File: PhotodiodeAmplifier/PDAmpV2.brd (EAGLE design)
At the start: 50.8 x 30.1 mm, 21 parts, among them IC1 CA3140N, IC2 7812L

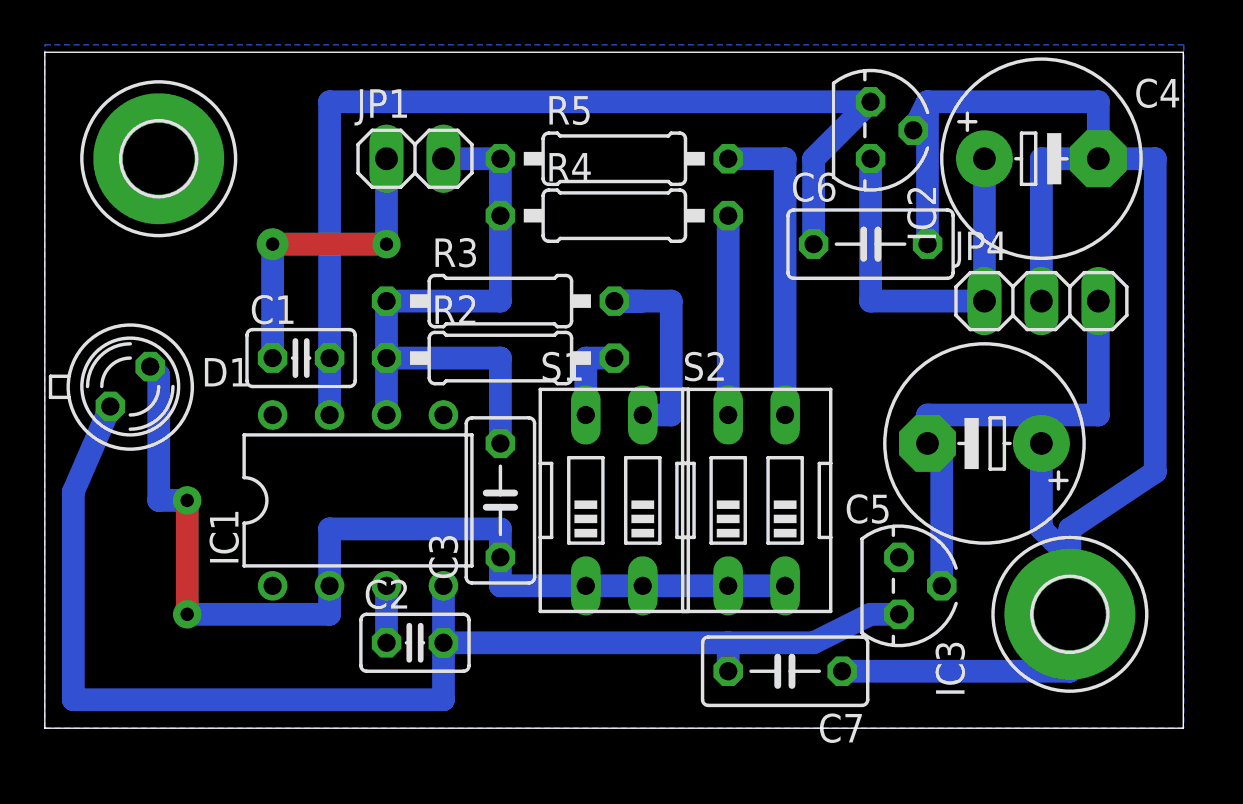
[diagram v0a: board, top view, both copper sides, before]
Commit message: Insert 50 ohm resistor into output
This actually makes the circuit work properly, previously I was doing this
with a terminator, but that's a bit dangerous for your ICS
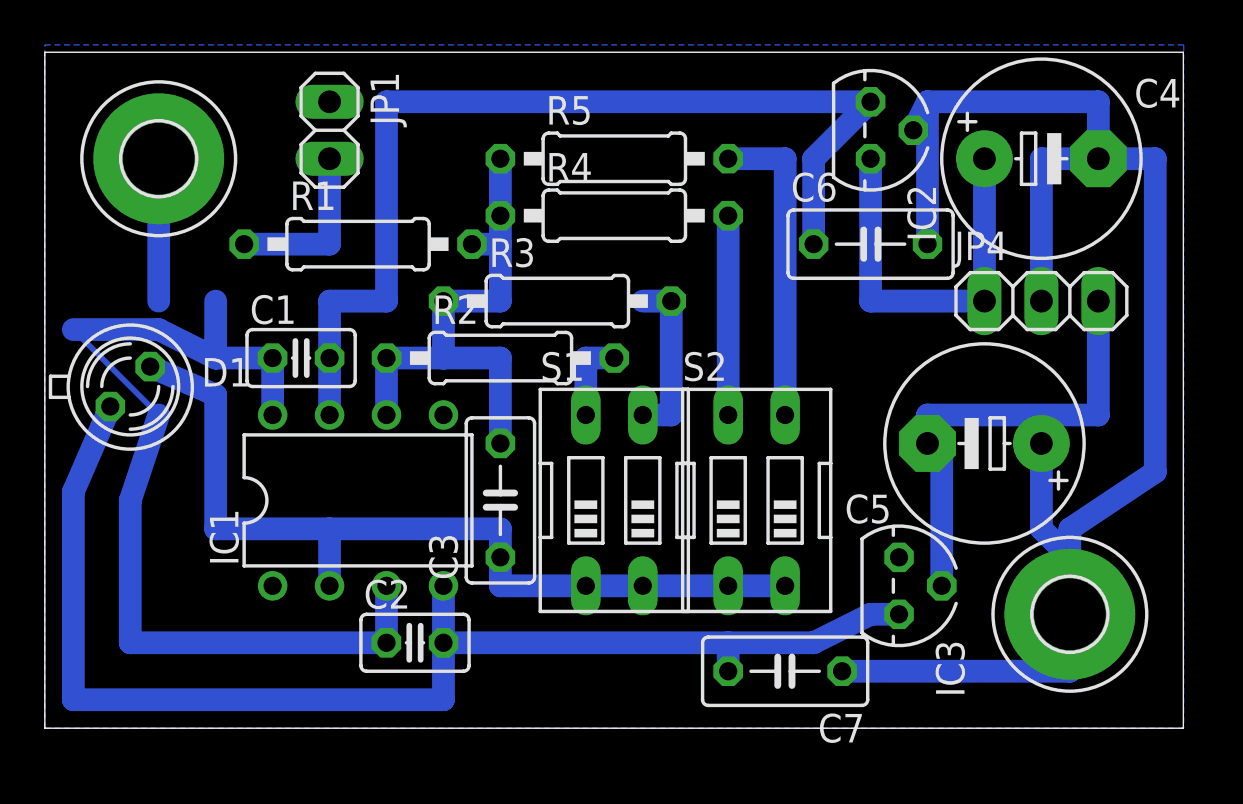
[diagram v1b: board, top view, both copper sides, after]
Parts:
- added R1: (no value), resistor:0207/10
- moved JP1 4.02 mm to (12.7, 26.7), turned to 270 degrees
- moved R3 2.54 mm to (22.9, 19.1)
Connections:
- new net N$10: JP1.2, R1.1
- net N$16: now also R1.2; no longer JP1.2
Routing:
- net GND: track 89.1 -> 122.9 mm
- net N$10: track 0.00 -> 7.62 mm
- net N$4: track 45.5 -> 39.6 mm
- net N$16: track 27.9 -> 24.1 mm
- net N$13: track 10.2 -> 7.62 mm
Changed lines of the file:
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@@
 </autorouter>
 <elements>
-<element name="JP1" library="pinhead" package="1X02" value="" x="16.51" y="25.4"/>
+<element name="JP1" library="pinhead" package="1X02" value="" x="12.7" y="26.67" rot="R270"/>
 <element name="GND" library="holes" package="3,2-PAD" value="MOUNT-PAD-ROUND3.2" x="5.08" y="25.4"/>
 <element name="H2" library="holes" package="3,2-PAD" value="MOUNT-PAD-ROUND3.2" x="45.72" y="5.08"/>
@@
 <element name="C3" library="rcl" package="C050-030X075" value="" x="20.32" y="10.16" rot="R90"/>
 <element name="R2" library="resistor" package="0207/10" value="" x="20.32" y="16.51"/>
-<element name="R3" library="resistor" package="0207/10" value="" x="20.32" y="19.05"/>
+<element name="R3" library="resistor" package="0207/10" value="" x="22.86" y="19.05"/>
 <element name="R4" library="resistor" package="0207/10" value="" x="25.4" y="22.86"/>
 <element name="R5" library="resistor" package="0207/10" value="" x="25.4" y="25.4"/>
+<element name="R1" library="resistor" package="0207/10" value="" x="13.97" y="21.59"/>
 </elements>
 <signals>
@@
 <contactref element="H2" pad="B3,2"/>
 <contactref element="JP1" pad="1"/>
-<wire x1="15.24" y1="6.35" x2="15.24" y2="3.81" width="1.016" layer="16"/>
 <wire x1="38.735" y1="26.67" x2="39.37" y2="27.94" width="1.016" layer="16"/>
 <polygon width="0.8128" layer="16">
@@
 <wire x1="49.53" y1="11.43" x2="49.53" y2="25.4" width="1.016" layer="16"/>
 <wire x1="49.53" y1="25.4" x2="46.99" y2="25.4" width="1.016" layer="16"/>
-<wire x1="15.24" y1="21.59" x2="10.16" y2="21.59" width="1.016" layer="1"/>
-<wire x1="10.16" y1="16.51" x2="10.16" y2="21.59" width="1.016" layer="16"/>
-<wire x1="15.24" y1="25.4" x2="15.24" y2="21.59" width="1.016" layer="16"/>
 <wire x1="44.45" y1="12.7" x2="44.45" y2="8.89" width="1.016" layer="16"/>
 <wire x1="44.45" y1="8.89" x2="45.72" y2="7.62" width="1.016" layer="16"/>
 <wire x1="45.72" y1="7.62" x2="45.72" y2="5.08" width="1.016" layer="16"/>
-<wire x1="10.16" y1="21.59" x2="10.16" y2="21.59" width="0" layer="19" extent="1-16"/>
-<wire x1="15.24" y1="21.59" x2="15.24" y2="21.59" width="0" layer="19" extent="1-16"/>
+<wire x1="10.16" y1="13.97" x2="10.16" y2="16.51" width="1.016" layer="16"/>
+<wire x1="10.16" y1="16.51" x2="7.62" y2="16.51" width="1.016" layer="16"/>
+<wire x1="7.62" y1="16.51" x2="7.62" y2="19.05" width="1.016" layer="16"/>
+<wire x1="5.08" y1="19.05" x2="5.08" y2="25.4" width="1.016" layer="16"/>
+<wire x1="15.24" y1="6.35" x2="15.24" y2="3.81" width="1.016" layer="16"/>
+<wire x1="15.24" y1="3.81" x2="3.81" y2="3.81" width="1.016" layer="16"/>
+<wire x1="3.81" y1="3.81" x2="3.81" y2="10.16" width="1.016" layer="16"/>
+<wire x1="7.62" y1="16.51" x2="5.08" y2="17.78" width="1.016" layer="16"/>
+<wire x1="5.08" y1="17.78" x2="1.27" y2="17.78" width="1.016" layer="16"/>
+<wire x1="1.27" y1="17.78" x2="5.08" y2="13.97" width="0.254" layer="16"/>
+<wire x1="5.08" y1="13.97" x2="3.81" y2="10.16" width="1.016" layer="16"/>
 </signal>
 <signal name="N$7">
@@
 <wire x1="17.78" y1="6.35" x2="17.78" y2="3.81" width="1.016" layer="16"/>
 <wire x1="17.78" y1="3.81" x2="17.78" y2="1.27" width="1.016" layer="16"/>
-<wire x1="1.27" y1="1.27" x2="17.78" y2="1.27" width="1.016" layer="16"/>
 <wire x1="2.921" y1="14.351" x2="1.27" y2="10.541" width="1.016" layer="16"/>
 <wire x1="1.27" y1="10.541" x2="1.27" y2="1.27" width="1.016" layer="16"/>
@@
 <wire x1="34.29" y1="3.81" x2="36.83" y2="5.08" width="1.016" layer="16"/>
 <wire x1="36.83" y1="5.08" x2="38.1" y2="5.08" width="1.016" layer="16"/>
+<wire x1="17.78" y1="1.27" x2="1.27" y2="1.27" width="1.016" layer="16"/>
 </signal>
 <signal name="+12V">
@@
 <contactref element="IC1" pad="7"/>
 <contactref element="C1" pad="2"/>
-<wire x1="36.83" y1="27.94" x2="12.7" y2="27.94" width="1.016" layer="16"/>
-<wire x1="12.7" y1="27.94" x2="12.7" y2="16.51" width="1.016" layer="16"/>
 <wire x1="12.7" y1="13.97" x2="12.7" y2="16.51" width="1.016" layer="16"/>
 <wire x1="36.83" y1="27.94" x2="34.29" y2="25.4" width="1.016" layer="16"/>
 <wire x1="34.29" y1="25.4" x2="34.29" y2="21.59" width="1.016" layer="16"/>
+<wire x1="36.83" y1="27.94" x2="15.24" y2="27.94" width="1.016" layer="16"/>
+<wire x1="12.7" y1="16.51" x2="12.7" y2="19.05" width="1.016" layer="16"/>
+<wire x1="12.7" y1="19.05" x2="15.24" y2="19.05" width="1.016" layer="16"/>
+<wire x1="15.24" y1="19.05" x2="15.24" y2="27.94" width="1.016" layer="16"/>
 </signal>
 <signal name="N$4">
@@
 <wire x1="26.67" y1="6.35" x2="30.48" y2="6.35" width="1.016" layer="16"/>
 <wire x1="30.48" y1="6.35" x2="33.02" y2="6.35" width="1.016" layer="16"/>
+<contactref element="D1" pad="K"/>
+<wire x1="20.32" y1="7.62" x2="20.32" y2="6.35" width="1.016" layer="16"/>
+<wire x1="20.32" y1="6.35" x2="24.13" y2="6.35" width="1.016" layer="16"/>
+<wire x1="4.699" y1="16.129" x2="7.62" y2="14.859" width="1.016" layer="16"/>
+<wire x1="7.62" y1="14.859" x2="7.62" y2="8.89" width="1.016" layer="16"/>
+<wire x1="7.62" y1="8.89" x2="12.7" y2="8.89" width="1.016" layer="16"/>
 <wire x1="12.7" y1="6.35" x2="12.7" y2="8.89" width="1.016" layer="16"/>
 <wire x1="12.7" y1="8.89" x2="20.32" y2="8.89" width="1.016" layer="16"/>
 <wire x1="20.32" y1="8.89" x2="20.32" y2="7.62" width="1.016" layer="16"/>
-<contactref element="D1" pad="K"/>
-<wire x1="20.32" y1="7.62" x2="20.32" y2="6.35" width="1.016" layer="16"/>
-<wire x1="20.32" y1="6.35" x2="24.13" y2="6.35" width="1.016" layer="16"/>
-<wire x1="4.699" y1="16.129" x2="5.08" y2="15.748" width="1.016" layer="16"/>
-<wire x1="12.7" y1="6.35" x2="12.7" y2="5.08" width="1.016" layer="16"/>
-<wire x1="5.08" y1="15.748" x2="5.08" y2="10.16" width="1.016" layer="16"/>
-<wire x1="6.35" y1="10.16" x2="6.35" y2="10.16" width="0" layer="19" extent="1-16"/>
-<wire x1="12.7" y1="5.08" x2="6.35" y2="5.08" width="1.016" layer="16"/>
-<wire x1="6.35" y1="5.08" x2="6.35" y2="5.08" width="0" layer="19" extent="1-16"/>
-<wire x1="5.08" y1="10.16" x2="6.35" y2="10.16" width="1.016" layer="16"/>
-<wire x1="6.35" y1="10.16" x2="6.35" y2="5.08" width="1.016" layer="1"/>
 </signal>
 <signal name="N$12">
@@
 <contactref element="R3" pad="2"/>
 <contactref element="S1" pad="3"/>
-<wire x1="26.67" y1="19.05" x2="25.4" y2="19.05" width="1.016" layer="16"/>
 <wire x1="26.67" y1="13.97" x2="27.94" y2="13.97" width="1.016" layer="16"/>
 <wire x1="27.94" y1="13.97" x2="27.94" y2="19.05" width="1.016" layer="16"/>
-<wire x1="27.94" y1="19.05" x2="25.4" y2="19.05" width="1.016" layer="16"/>
+<wire x1="26.67" y1="19.05" x2="27.94" y2="19.05" width="1.016" layer="16"/>
 </signal>
 <signal name="N$14">
@@
 <contactref element="R3" pad="1"/>
 <contactref element="IC1" pad="6"/>
-<contactref element="JP1" pad="2"/>
 <contactref element="C3" pad="2"/>
 <contactref element="R4" pad="1"/>
@@
 <contactref element="R2" pad="1"/>
 <wire x1="15.24" y1="16.51" x2="15.24" y2="13.97" width="1.016" layer="16"/>
-<wire x1="15.24" y1="16.51" x2="15.24" y2="19.05" width="1.016" layer="16"/>
 <wire x1="20.32" y1="22.86" x2="20.32" y2="25.4" width="1.016" layer="16"/>
-<wire x1="15.24" y1="16.51" x2="20.32" y2="16.51" width="1.016" layer="16"/>
+<wire x1="15.24" y1="16.51" x2="17.78" y2="16.51" width="1.016" layer="16"/>
+<wire x1="17.78" y1="16.51" x2="20.32" y2="16.51" width="1.016" layer="16"/>
 <wire x1="20.32" y1="16.51" x2="20.32" y2="12.7" width="1.016" layer="16"/>
-<wire x1="17.78" y1="25.4" x2="20.32" y2="25.4" width="1.016" layer="16"/>
-<wire x1="20.32" y1="22.86" x2="20.32" y2="19.05" width="1.016" layer="16"/>
-<wire x1="20.32" y1="19.05" x2="15.24" y2="19.05" width="1.016" layer="16"/>
+<contactref element="R1" pad="2"/>
+<wire x1="20.32" y1="22.86" x2="20.32" y2="21.59" width="1.016" layer="16"/>
+<wire x1="20.32" y1="21.59" x2="20.32" y2="19.05" width="1.016" layer="16"/>
+<wire x1="20.32" y1="19.05" x2="17.78" y2="19.05" width="1.016" layer="16"/>
+<wire x1="17.78" y1="19.05" x2="17.78" y2="16.51" width="1.016" layer="16"/>
+<wire x1="19.05" y1="21.59" x2="20.32" y2="21.59" width="1.016" layer="16"/>
 </signal>
 <signal name="N$2">
@@
 </signal>
 <signal name="N$1">
-<via x="6.35" y="5.08" extent="1-16" drill="0.6" diameter="1.27"/>
 </signal>
 <signal name="N$5">
-<via x="6.35" y="10.16" extent="1-16" drill="0.6" diameter="1.27"/>
 </signal>
 <signal name="N$6">
-<via x="15.24" y="21.59" extent="1-16" drill="0.6" diameter="1.27"/>
 </signal>
 <signal name="N$8">
-<via x="10.16" y="21.59" extent="1-16" drill="0.6" diameter="1.4224"/>
+</signal>
+<signal name="N$10">
+<contactref element="JP1" pad="2"/>
+<contactref element="R1" pad="1"/>
+<wire x1="12.7" y1="25.4" x2="12.7" y2="21.59" width="1.016" layer="16"/>
+<wire x1="12.7" y1="21.59" x2="8.89" y2="21.59" width="1.016" layer="16"/>
 </signal>
 </signals>
